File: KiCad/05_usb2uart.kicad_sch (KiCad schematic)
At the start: 18 parts, among them IC501 FT232RL-REEL, J501 Conn_01x09_Pin, J502 Conn_01x09_Pin, J503 Conn_01x06_Pin, J504 USB_C_Receptacle_USB2.0_16P, U501 USBLC6-2SC6

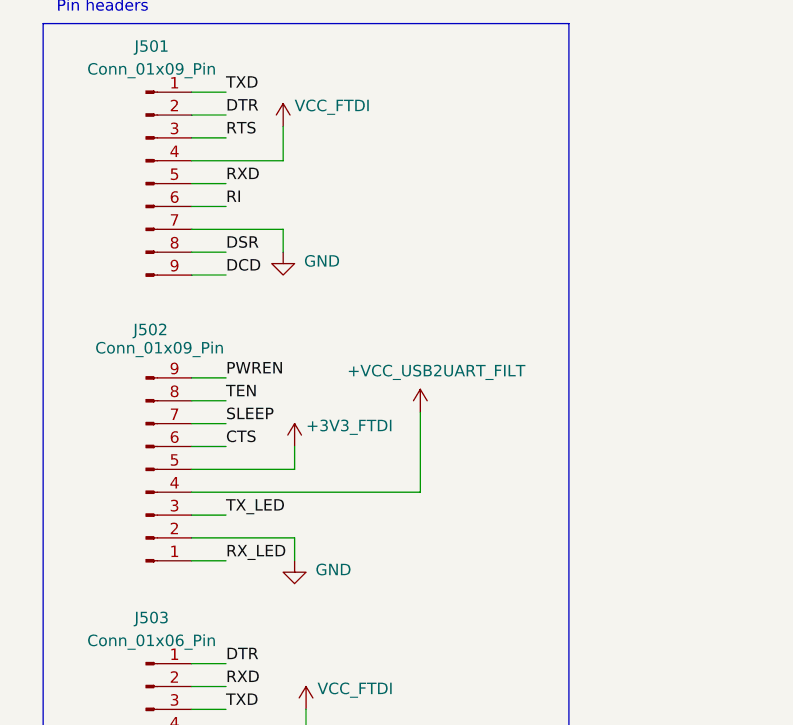
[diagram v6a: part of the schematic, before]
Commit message: PCB UART routing
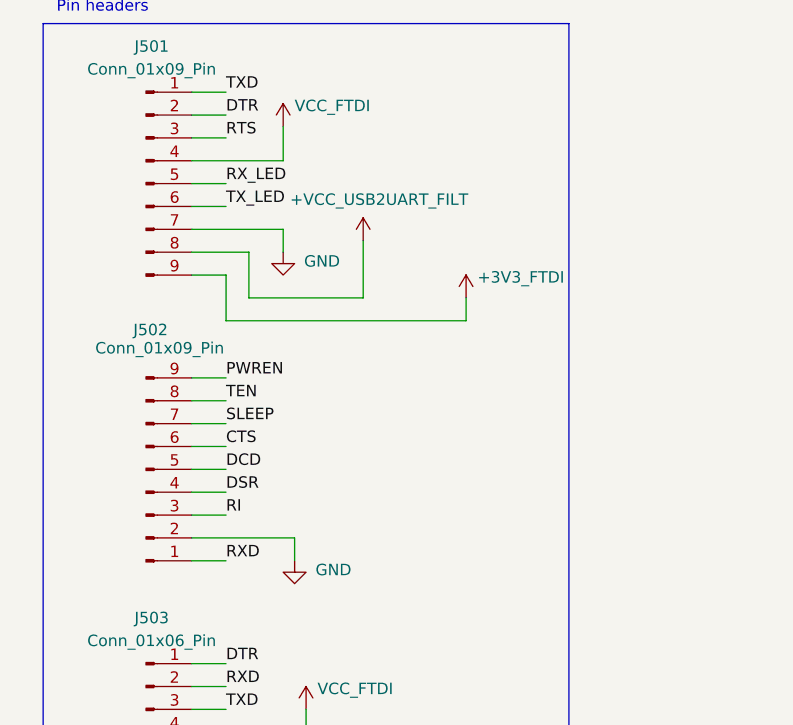
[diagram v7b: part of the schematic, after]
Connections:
- net +3V3_FTDI: now also J501.9 (Pin_9); no longer J502.5 (Pin_5)
- net +VCC_USB2UART_FILT: now also J501.8 (Pin_8); no longer J502.4 (Pin_4)
- net DCD: now also J502.5 (Pin_5); no longer J501.9 (Pin_9)
- net DSR: now also J502.4 (Pin_4); no longer J501.8 (Pin_8)
- net RI: now also J502.3 (Pin_3); no longer J501.6 (Pin_6)
- net RXD: now also J502.1 (Pin_1); no longer J501.5 (Pin_5)
- net RX_LED: now also J501.5 (Pin_5); no longer J502.1 (Pin_1)
- net TX_LED: now also J501.6 (Pin_6); no longer J502.3 (Pin_3)
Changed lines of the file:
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@@
 	(wire
 		(pts
-			(xy 30.48 87.63) (xy 41.91 87.63)
-		)
-		(stroke
-			(width 0)
-			(type default)
-		)
-	)
-	(wire
-		(pts
 			(xy 43.18 144.78) (xy 52.07 144.78)
 		)
@@
 	(wire
 		(pts
-			(xy 41.91 87.63) (xy 41.91 85.09)
+			(xy 35.56 184.15) (xy 43.18 184.15)
 		)
 		(stroke
@@
 	(wire
 		(pts
-			(xy 35.56 184.15) (xy 43.18 184.15)
+			(xy 36.83 63.5) (xy 36.83 68.58)
 		)
 		(stroke
@@
 	(wire
 		(pts
-			(xy 30.48 90.17) (xy 55.88 90.17)
-		)
-		(stroke
-			(width 0)
-			(type default)
-		)
-	)
-	(wire
-		(pts
 			(xy 109.22 57.15) (xy 121.92 57.15)
 		)
@@
 	(wire
 		(pts
+			(xy 34.29 71.12) (xy 60.96 71.12)
+		)
+		(stroke
+			(width 0)
+			(type default)
+		)
+	)
+	(wire
+		(pts
 			(xy 113.03 72.39) (xy 113.03 73.66)
 		)
@@
 	(wire
 		(pts
-			(xy 139.7 87.63) (xy 139.7 85.09)
+			(xy 60.96 68.58) (xy 60.96 71.12)
 		)
 		(stroke
@@
 	(wire
 		(pts
-			(xy 137.16 143.51) (xy 139.7 143.51)
+			(xy 139.7 87.63) (xy 139.7 85.09)
 		)
 		(stroke
@@
 	(wire
 		(pts
-			(xy 204.47 119.38) (xy 204.47 116.84)
+			(xy 137.16 143.51) (xy 139.7 143.51)
 		)
 		(stroke
@@
 	(wire
 		(pts
-			(xy 228.6 109.22) (xy 224.79 109.22)
+			(xy 204.47 119.38) (xy 204.47 116.84)
 		)
 		(stroke
@@
 	(wire
 		(pts
-			(xy 173.99 100.33) (xy 173.99 101.6)
+			(xy 228.6 109.22) (xy 224.79 109.22)
 		)
 		(stroke
@@
 	(wire
 		(pts
-			(xy 55.88 90.17) (xy 55.88 81.28)
+			(xy 173.99 100.33) (xy 173.99 101.6)
 		)
 		(stroke
@@
 	(wire
 		(pts
+			(xy 36.83 68.58) (xy 49.53 68.58)
+		)
+		(stroke
+			(width 0)
+			(type default)
+		)
+	)
+	(wire
+		(pts
+			(xy 34.29 66.04) (xy 34.29 71.12)
+		)
+		(stroke
+			(width 0)
+			(type default)
+		)
+	)
+	(wire
+		(pts
 			(xy 30.48 97.79) (xy 34.29 97.79)
 		)
@@
 	(wire
 		(pts
+			(xy 49.53 62.23) (xy 49.53 68.58)
+		)
+		(stroke
+			(width 0)
+			(type default)
+		)
+	)
+	(wire
+		(pts
 			(xy 121.92 46.99) (xy 139.7 46.99)
 		)
@@
 	(wire
 		(pts
-			(xy 30.48 63.5) (xy 34.29 63.5)
+			(xy 30.48 63.5) (xy 36.83 63.5)
 		)
 		(stroke
@@
 	(wire
 		(pts
+			(xy 30.48 87.63) (xy 34.29 87.63)
+		)
+		(stroke
+			(width 0)
+			(type default)
+		)
+	)
+	(wire
+		(pts
 			(xy 243.84 143.51) (xy 243.84 142.24)
 		)
@@
 	(wire
 		(pts
+			(xy 30.48 90.17) (xy 34.29 90.17)
+		)
+		(stroke
+			(width 0)
+			(type default)
+		)
+	)
+	(wire
+		(pts
 			(xy 109.22 73.66) (xy 109.22 74.93)
 		)
@@
 		)
 	)
-	(label "RXD"
-		(at 34.29 55.88 0)
+	(label "RI"
+		(at 34.29 92.71 0)
 		(effects
 			(font
@@
 		)
 	)
-	(label "USB2UART_CONN_D+"
-		(at 204.47 124.46 0)
+	(label "TX_LED"
+		(at 34.29 58.42 0)
 		(effects
 			(font
@@
 		)
 	)
-	(label "PWREN"
-		(at 109.22 124.46 0)
+	(label "DCD"
+		(at 34.29 87.63 0)
 		(effects
 			(font
@@
 		)
 	)
-	(label "DTR"
-		(at 109.22 100.33 0)
+	(label "USB2UART_CONN_D+"
+		(at 204.47 124.46 0)
 		(effects
 			(font
@@
 		)
 	)
-	(label "RI"
-		(at 109.22 105.41 0)
+	(label "DSR"
+		(at 34.29 90.17 0)
 		(effects
 			(font
@@
 		)
 	)
-	(label "USB2UART_CONN_CC2"
-		(at 201.93 96.52 0)
+	(label "PWREN"
+		(at 109.22 124.46 0)
 		(effects
 			(font
@@
 		)
 	)
-	(label "TX_LED"
-		(at 34.29 92.71 0)
+	(label "DTR"
+		(at 109.22 100.33 0)
 		(effects
 			(font
@@
 		)
 	)
-	(label "DTR"
-		(at 34.29 48.26 0)
+	(label "RI"
+		(at 109.22 105.41 0)
 		(effects
 			(font
@@
 		)
 	)
-	(label "RI"
-		(at 34.29 58.42 0)
+	(label "USB2UART_CONN_CC2"
+		(at 201.93 96.52 0)
+		(effects
+			(font
+				(size 1.27 1.27)
+			)
+			(justify left bottom)
+		)
+	)
+	(label "DTR"
+		(at 34.29 48.26 0)
 		(effects
 			(font
@@
 		)
 	)
+	(label "RX_LED"
+		(at 34.29 55.88 0)
+		(effects
+			(font
+				(size 1.27 1.27)
+			)
+			(justify left bottom)
+		)
+	)
 	(label "TX_LED"
 		(at 52.07 151.13 0)
@@
 		)
 	)
-	(label "DSR"
-		(at 34.29 63.5 0)
-		(effects
-			(font
-				(size 1.27 1.27)
-			)
-			(justify left bottom)
-		)
-	)
 	(label "RX_LED"
 		(at 109.22 116.84 0)
@@
 		)
 	)
-	(label "RX_LED"
-		(at 34.29 97.79 0)
-		(effects
-			(font
-				(size 1.27 1.27)
-			)
-			(justify left bottom)
-		)
-	)
 	(label "TXD"
 		(at 34.29 45.72 0)
@@
 		)
 	)
-	(label "DCD"
-		(at 34.29 66.04 0)
+	(label "RXD"
+		(at 34.29 97.79 0)
 		(effects
 			(font
@@
 	(symbol
 		(lib_id "power:+5V")
-		(at 55.88 81.28 0)
+		(at 49.53 62.23 0)
 		(unit 1)
 		(exclude_from_sim no)
@@
 		(dnp no)
 		(property "Reference" "#PWR0506"
-			(at 55.88 85.09 0)
+			(at 49.53 66.04 0)
 			(effects
 				(font
@@
 		)
 		(property "Value" "+VCC_USB2UART_FILT"
-			(at 47.752 76.708 0)
+			(at 41.402 57.658 0)
 			(effects
 				(font
@@
 		)
 		(property "Footprint" ""
-			(at 55.88 81.28 0)
+			(at 49.53 62.23 0)
 			(effects
 				(font
@@
 		)
 		(property "Datasheet" ""
-			(at 55.88 81.28 0)
+			(at 49.53 62.23 0)
 			(effects
 				(font
@@
 		)
 		(property "Description" "Power symbol creates a global label with name \"+5V\""
-			(at 55.88 81.28 0)
+			(at 49.53 62.23 0)
 			(effects
 				(font
@@
 	(symbol
 		(lib_id "power:+5V")
-		(at 41.91 85.09 0)
+		(at 60.96 68.58 0)
 		(unit 1)
 		(exclude_from_sim no)
@@
 		(dnp no)
 		(property "Reference" "#PWR0507"
-			(at 41.91 88.9 0)
+			(at 60.96 72.39 0)
 			(effects
 				(font
@@
 		)
 		(property "Value" "+3V3_FTDI"
-			(at 43.18 82.804 0)
+			(at 62.23 66.294 0)
 			(effects
 				(font
@@
 		)
 		(property "Footprint" ""
-			(at 41.91 85.09 0)
+			(at 60.96 68.58 0)
 			(effects
 				(font
@@
 		)
 		(property "Datasheet" ""
-			(at 41.91 85.09 0)
+			(at 60.96 68.58 0)
 			(effects
 				(font
@@
 		)
 		(property "Description" "Power symbol creates a global label with name \"+5V\""
-			(at 41.91 85.09 0)
+			(at 60.96 68.58 0)
 			(effects
 				(font

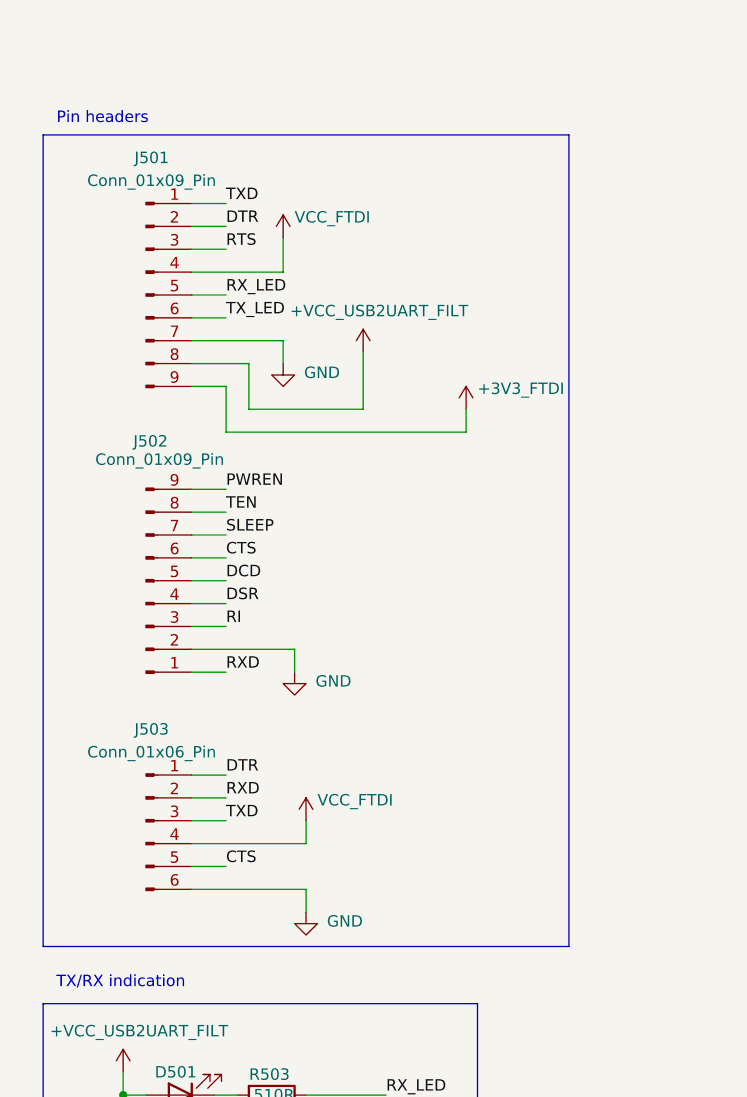
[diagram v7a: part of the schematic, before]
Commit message: Update FTDI pinout
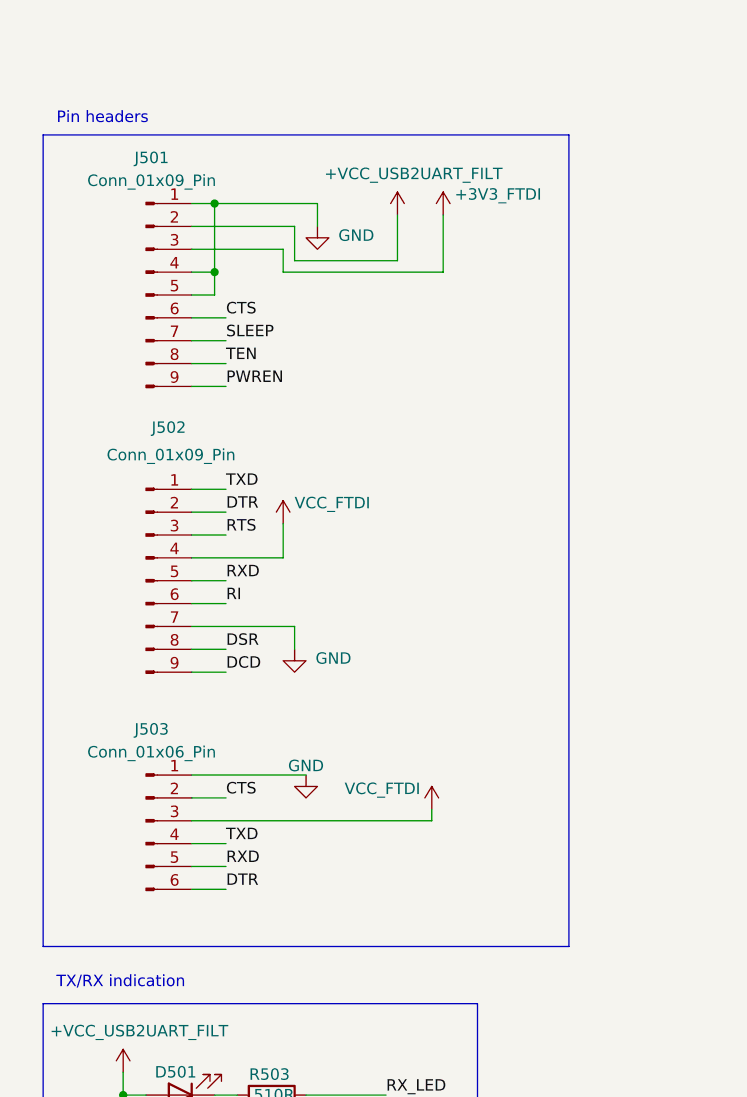
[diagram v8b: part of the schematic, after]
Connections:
- net +3V3_FTDI: now also J501.3 (Pin_3); no longer J501.9 (Pin_9)
- net +VCC_USB2UART_FILT: now also J501.2 (Pin_2); no longer J501.8 (Pin_8)
- net CTS: now also J501.6 (Pin_6), J503.2 (Pin_2); no longer J502.6 (Pin_6), J503.5 (Pin_5)
- net DCD: now also J502.9 (Pin_9); no longer J502.5 (Pin_5)
- net DSR: now also J502.8 (Pin_8); no longer J502.4 (Pin_4)
- net DTR: now also J502.2 (Pin_2), J503.6 (Pin_6); no longer J501.2 (Pin_2), J503.1 (Pin_1)
- net GND: now also J501.1 (Pin_1), J501.4 (Pin_4), J501.5 (Pin_5), J502.7 (Pin_7), J503.1 (Pin_1); no longer J501.7 (Pin_7), J502.2 (Pin_2), J503.6 (Pin_6)
- net PWREN: now also J501.9 (Pin_9); no longer J502.9 (Pin_9)
- net RI: now also J502.6 (Pin_6); no longer J502.3 (Pin_3)
- net RTS: now also J502.3 (Pin_3); no longer J501.3 (Pin_3)
- net RXD: now also J502.5 (Pin_5), J503.5 (Pin_5); no longer J502.1 (Pin_1), J503.2 (Pin_2)
- net RX_LED: no longer J501.5 (Pin_5)
- net SLEEP: now also J501.7 (Pin_7); no longer J502.7 (Pin_7)
- net TEN: now also J501.8 (Pin_8); no longer J502.8 (Pin_8)
- net TXD: now also J502.1 (Pin_1), J503.4 (Pin_4); no longer J501.1 (Pin_1), J503.3 (Pin_3)
- net TX_LED: no longer J501.6 (Pin_6)
- net VCC_FTDI: now also J502.4 (Pin_4), J503.3 (Pin_3); no longer J501.4 (Pin_4), J503.4 (Pin_4)
